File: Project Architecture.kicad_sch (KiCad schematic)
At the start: 0 parts

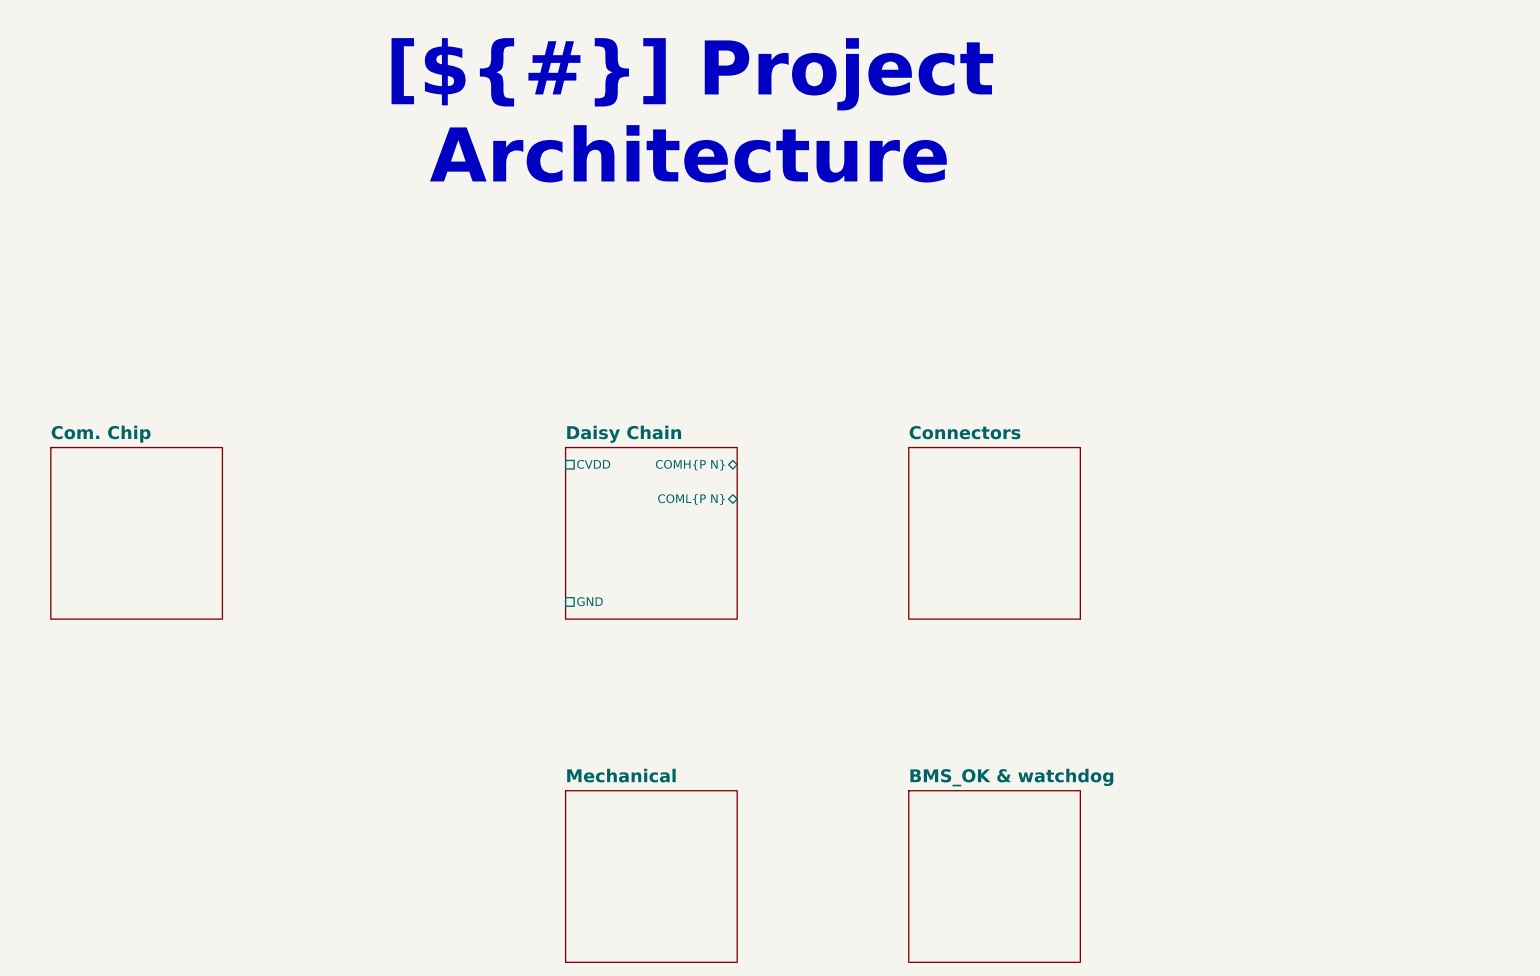
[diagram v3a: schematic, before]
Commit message: SCH[Sens & Inputs, Logic]: Started on sens and inputs condtiong, Logic page drawn. Need to add notes still.
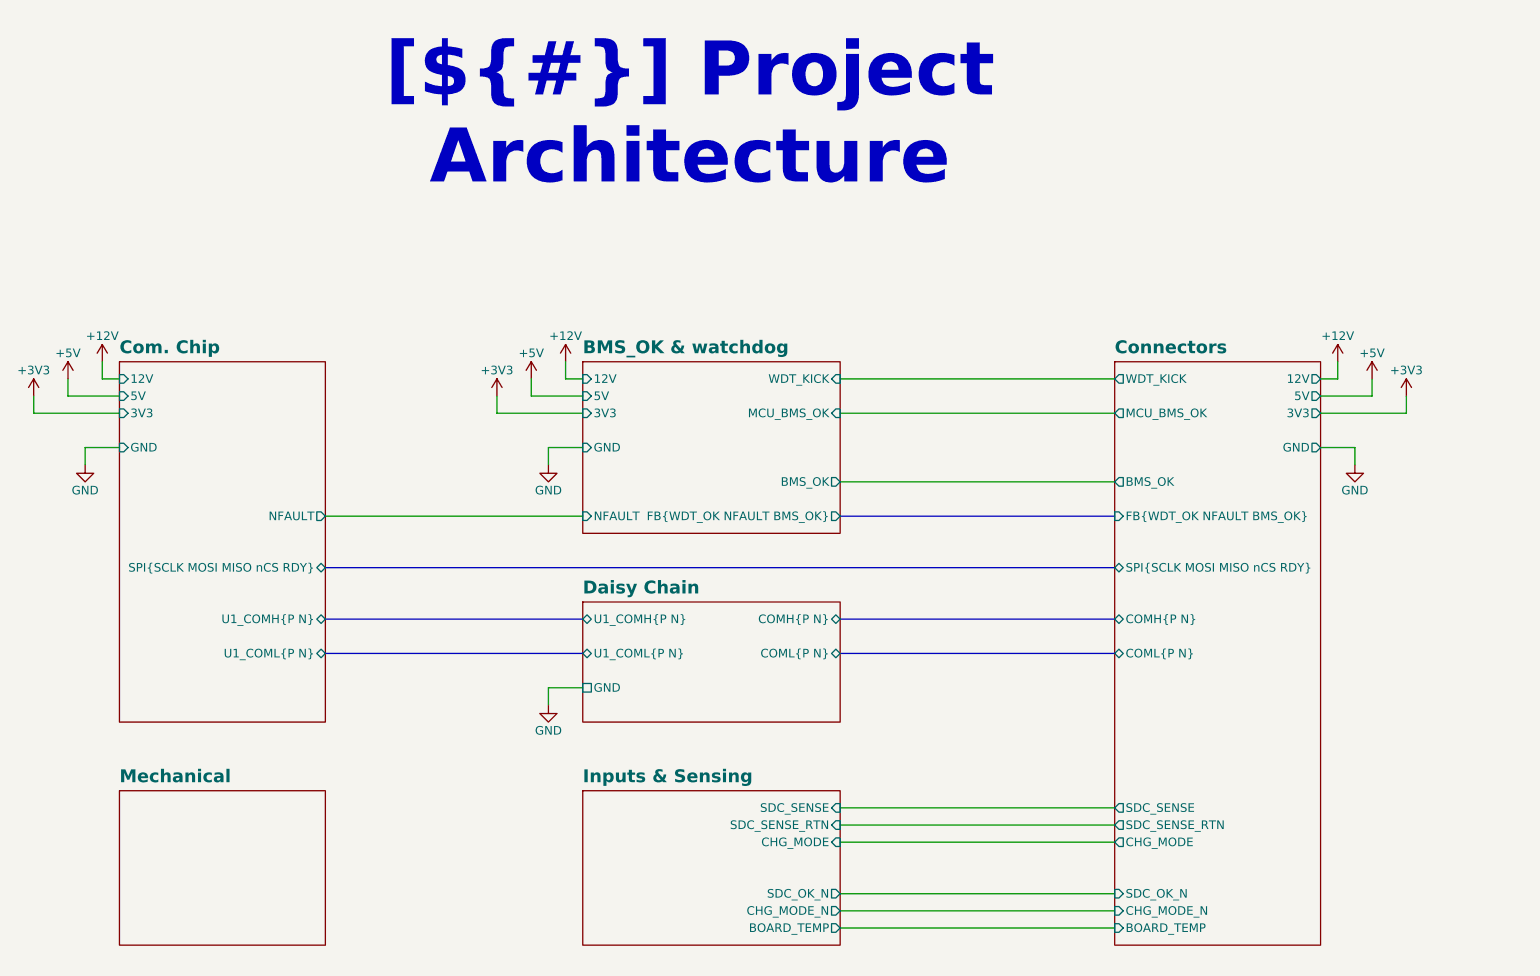
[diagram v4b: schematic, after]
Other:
- added sheet Inputs & Sensing (inputs_and_sensing.kicad_sch)
- sheet BMS_OK & watchdog ports: added 12V, 3V3, 5V, BMS_OK, FB{WDT_OK NFAULT BMS_OK}, GND, MCU_BMS_OK, NFAULT, WDT_KICK; removed none
- sheet Com. Chip ports: added 12V, 3V3, 5V, GND, NFAULT, SPI{SCLK MOSI MISO nCS RDY}, U1_COMH{P N}, U1_COML{P N}; removed none
- sheet Connectors ports: added 12V, 3V3, 5V, BMS_OK, BOARD_TEMP, CHG_MODE, CHG_MODE_N, COMH{P N}, COML{P N}, FB{WDT_OK NFAULT BMS_OK}, GND, MCU_BMS_OK, SDC_OK_N, SDC_SENSE, SDC_SENSE_RTN, SPI{SCLK MOSI MISO nCS RDY}, WDT_KICK; removed none
- sheet Daisy Chain ports: added U1_COMH{P N}, U1_COML{P N}; removed CVDD

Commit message: PCB[Daisy]: Inital layout for this.
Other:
- sheet BMS_OK & watchdog renamed BMS_OK & Indicators
- sheet BMS_OK & Indicators: file bms_ok_and_watchdog.kicad_sch -> bms_ok_and_indicators.kicad_sch
- sheet BMS_OK & Indicators ports: added FB{NFAULT BMS_OK}; removed FB{WDT_OK NFAULT BMS_OK}
- sheet Connectors ports: added FB{NFAULT BMS_OK}; removed FB{WDT_OK NFAULT BMS_OK}
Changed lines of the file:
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@@
 			(color 255 255 194 1)
 		)
-		(property "Sheetname" "BMS_OK & watchdog"
+		(property "Sheetname" "BMS_OK & Indicators"
 			(at 129.54 62.4709 0)
 			(show_name no)
@@
 			)
 		)
-		(property "Sheetfile" "bms_ok_and_watchdog.kicad_sch"
+		(property "Sheetfile" "bms_ok_and_indicators.kicad_sch"
 			(at 129.54 89.4846 0)
 			(hide yes)
@@
 			)
 		)
-		(pin "FB{WDT_OK NFAULT BMS_OK}" output
+		(pin "FB{NFAULT BMS_OK}" output
 			(at 167.64 86.36 0)
 			(effects
@@
 			)
 		)
-		(pin "FB{WDT_OK NFAULT BMS_OK}" input
+		(pin "FB{NFAULT BMS_OK}" input
 			(at 208.28 86.36 180)
 			(effects

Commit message: PCB[Layout, Mounting]:Inital layout and edgecut/hole placment.
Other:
- sheet Inputs & Sensing ports: added 12V, 3V3, 5V, GND; removed none
